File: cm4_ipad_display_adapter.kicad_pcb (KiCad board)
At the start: 4 copper layers, 16 parts, among them J1 Conn_01x22_Female, J3 Conn_01x34_Female, J4 Conn_01x03_Female, U1 SN65DSI83TPAPRQ1, U2 MIC5504-1.8YM5

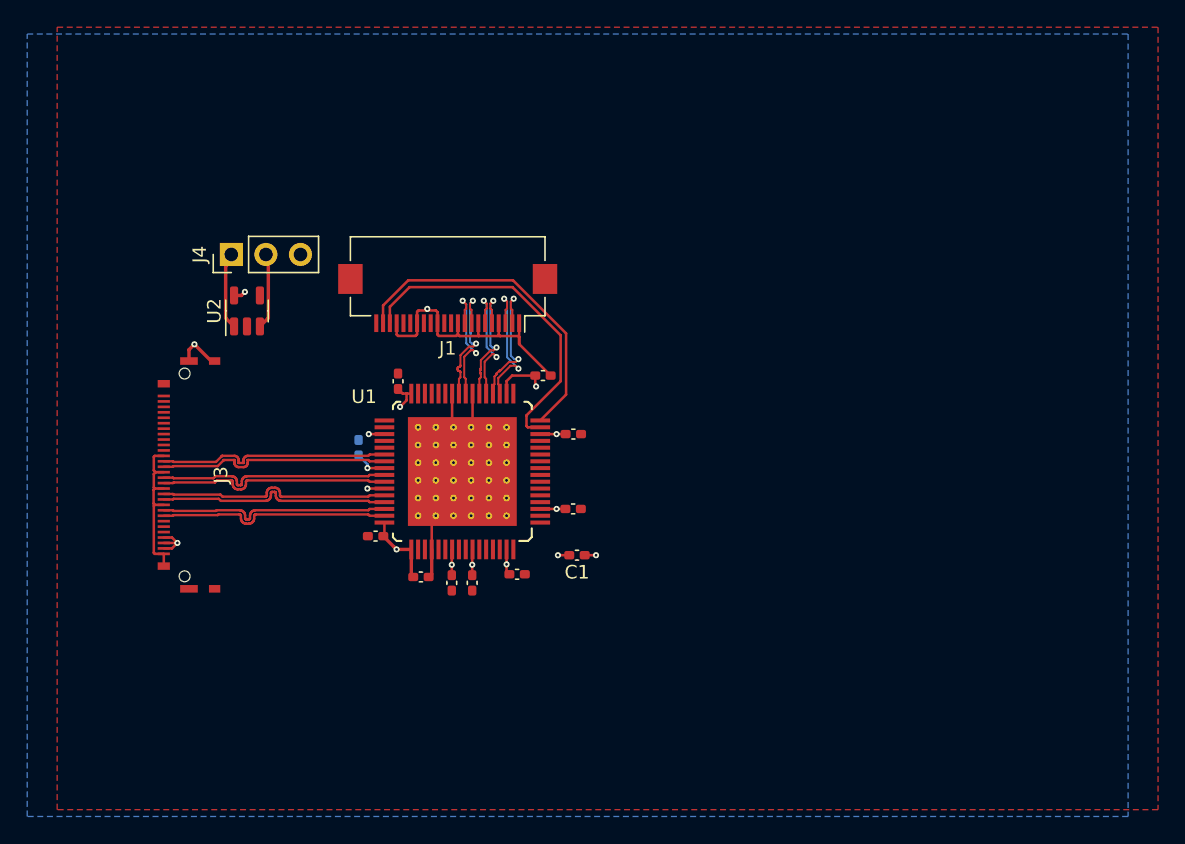
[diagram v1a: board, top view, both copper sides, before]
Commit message: Add footprints for LED driver HEAD associated components, route them. Fix DRC issues, and add an edge cut.
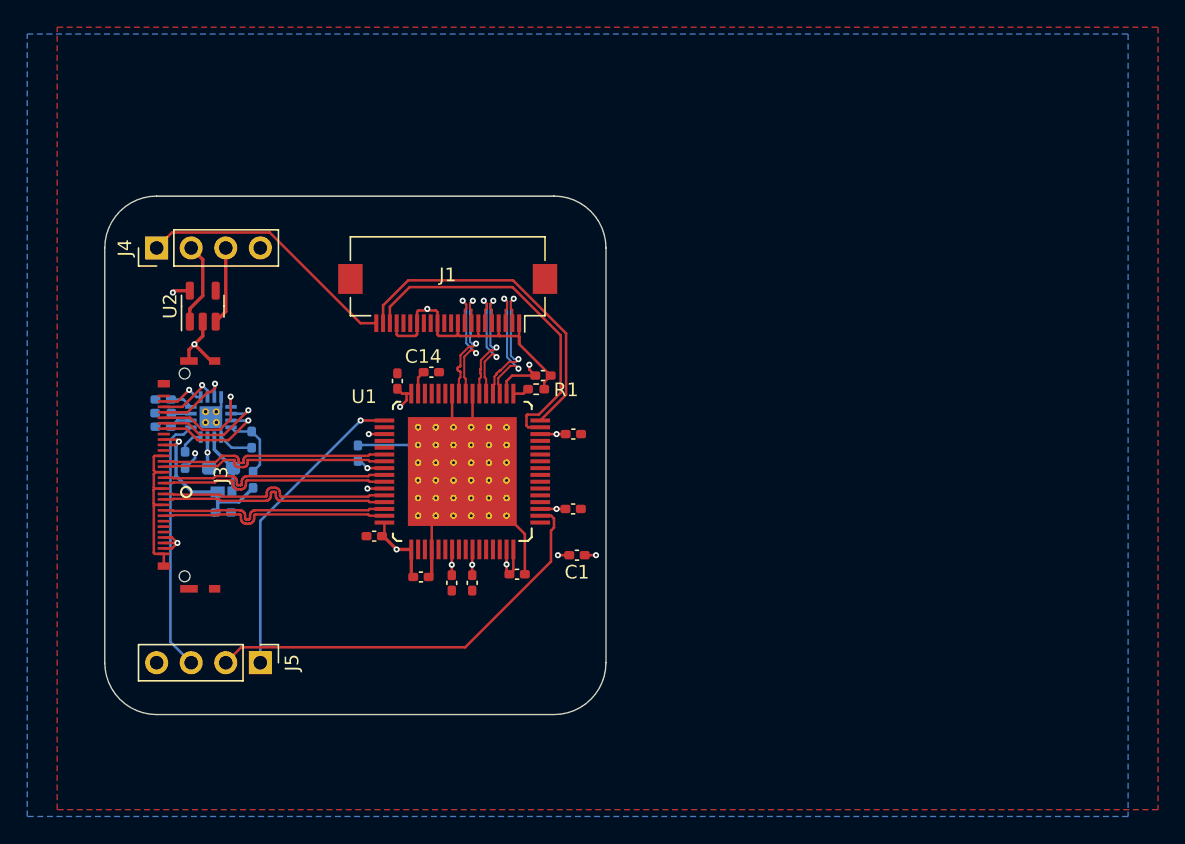
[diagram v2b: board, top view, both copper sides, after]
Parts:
- added C14: 1uF, Capacitor_SMD:C_0402_1005Metric_Pad0.74x0.62mm_HandSolder, F.Cu at (138.3, 54.9)
- added C15: 1uF, Capacitor_SMD:C_0402_1005Metric_Pad0.74x0.62mm_HandSolder, B.Cu at (118.6, 58.9)
- added C16: 0.47uF, Capacitor_SMD:C_0402_1005Metric_Pad0.74x0.62mm_HandSolder, B.Cu at (118.6, 56.9)
- added C17: 4.7uF, Capacitor_SMD:C_0402_1005Metric_Pad0.74x0.62mm_HandSolder, B.Cu at (123.0, 65.2)
- added D1: D_Schottky, footprints:PMEG4010EPK_315, B.Cu at (122.6, 63.7)
- added J5: Conn_01x04_Female, Connector_PinHeader_2.54mm:PinHeader_1x04_P2.54mm_Vertical, F.Cu at (125.7, 76.2)
- added L1: 4.7uH, Inductor_SMD:L_0603_1608Metric_Pad1.05x0.95mm_HandSolder, B.Cu at (122.8, 61.9)
- added R1: 10k, Resistor_SMD:R_0402_1005Metric_Pad0.72x0.64mm_HandSolder, F.Cu at (146.0, 56.1)
- added R2: 53.6k, Resistor_SMD:R_0402_1005Metric_Pad0.72x0.64mm_HandSolder, B.Cu at (118.6, 57.9)
- added R3: 1.3M, Resistor_SMD:R_0402_1005Metric_Pad0.72x0.64mm_HandSolder, B.Cu at (120.2, 61.3)
- added R4: 1M, Resistor_SMD:R_0402_1005Metric_Pad0.72x0.64mm_HandSolder, B.Cu at (125.2, 62.8)
- added R5: 143k, Resistor_SMD:R_0402_1005Metric_Pad0.72x0.64mm_HandSolder, B.Cu at (125.1, 59.8)
- added U3: TPS61176RTER, footprints:TPS61176RTER, B.Cu at (122.1, 58.1)
- J4: value Conn_01x03_Female -> Conn_01x02_Female; footprint Connector_PinHeader_2.54mm:PinHeader_1x03_P2.54mm_Vertical -> Connector_PinHeader_2.54mm:PinHeader_1x04_P2.54mm_Vertical
- U1: value SN65DSI83TPAPRQ1 -> PAP0064Q_N
- moved J4 5.51 mm to (118.1, 45.7)
- moved U2 3.27 mm to (121.5, 50.0)
- moved C5 0.40 mm to (132.9, 60.8)
- moved C2 0.10 mm to (134.1, 66.9)
- moved C4 0.05 mm to (135.8, 55.5)
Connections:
- J4 pad 2: Net-(J4-Pad2) -> VBAT
- J4 pad 3: GND -> LDO_EN
- U1 pad 17: unconnected-(U1-Pad17) -> Net-(R1-Pad1)
- U1 pad 2: unconnected-(U1-Pad2) -> Net-(J5-Pad2)
- U1 pad 31: unconnected-(U1-Pad31) -> Net-(C14-Pad1)
- U1 pad 33: unconnected-(U1-Pad33) -> Net-(J5-Pad1)
- U1 pad 64: unconnected-(U1-Pad64) -> VCC_1.8
- U2 pad 1: VCC_3.3 -> VBAT
- U2 pad 3: Net-(J4-Pad2) -> LDO_EN
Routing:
- net VCC_3.3: track 9.05 -> 45.0 mm
- net Net-(J5-Pad2): track 0.00 -> 31.3 mm
- net VBAT: track 0.00 -> 28.4 mm, vias 0 -> 1
- net Net-(J5-Pad1): track 0.00 -> 22.6 mm, vias 0 -> 1
- net PWM: track 0.00 -> 18.9 mm
- net GND: track 47.3 -> 66.2 mm, vias 3 -> 4
- net /LVDS/LED_ANODE: track 0.00 -> 13.8 mm, vias 0 -> 1
- net /LVDS/LED_CATHODE2: track 0.00 -> 8.70 mm, vias 0 -> 1
- net /LVDS/LED_CATHODE1: track 0.00 -> 8.44 mm, vias 0 -> 1
- net /LVDS/LED_CATHODE3: track 0.00 -> 8.01 mm, vias 0 -> 1
- net /LVDS/LED_CATHODE4: track 0.00 -> 5.81 mm, vias 0 -> 1
- net LDO_EN: track 0.00 -> 5.72 mm
- net Net-(J4-Pad2): track 5.62 -> 0.00 mm
- net Net-(R4-Pad2): track 0.00 -> 5.06 mm
- net Net-(L1-Pad2): track 0.00 -> 4.63 mm
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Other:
- board outline added: 36.8 x 38.1 mm

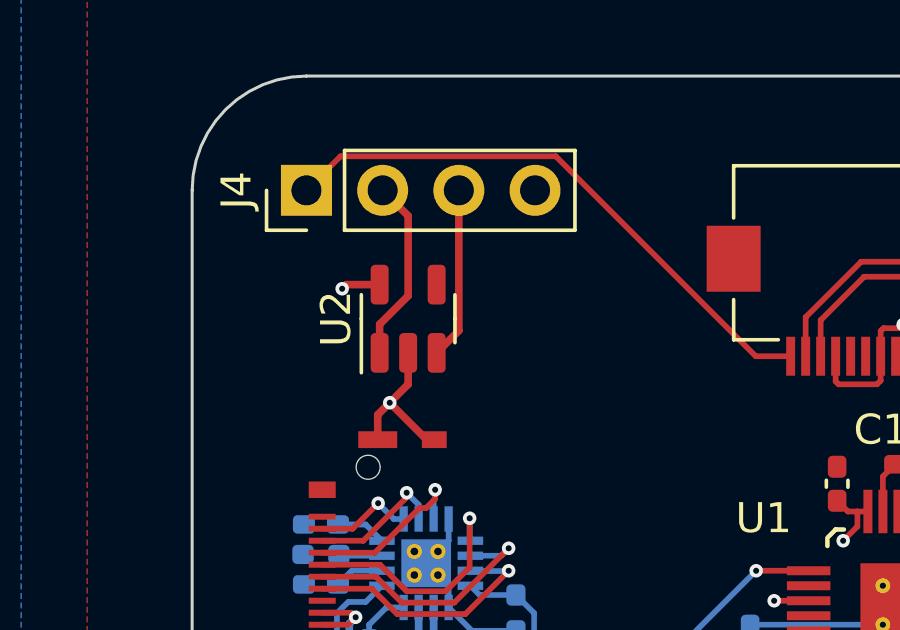
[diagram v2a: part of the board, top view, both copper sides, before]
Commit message: rearrange J4 pins to make traces for LDO simpler.
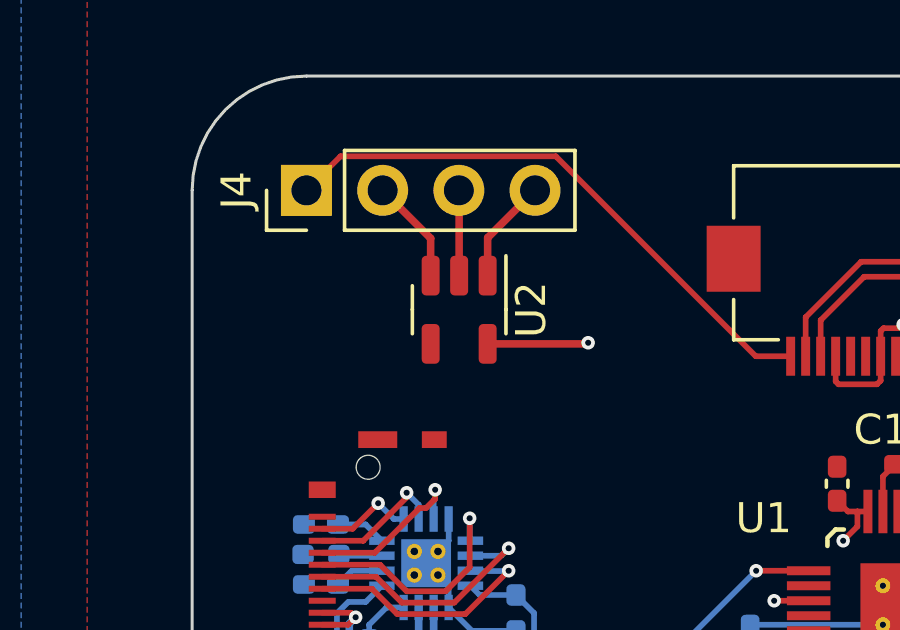
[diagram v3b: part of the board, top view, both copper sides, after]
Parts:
- U1: value PAP0064Q_N -> SN65DSI83TPAPRQ1
- moved U2 1.73 mm to (123.2, 49.7), turned to -90 degrees
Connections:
- net Net-(J5-Pad1) renamed /LVDS/IRQ
- net Net-(J5-Pad2) renamed /LVDS/SN65DSI83_EN
- J4 pad 2: VBAT -> LDO_EN
- J4 pad 3: LDO_EN -> GND
- J4 pad 4: GND -> VBAT
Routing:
- net VBAT: track 28.4 -> 23.7 mm
- net GND: track 66.2 -> 63.7 mm, vias 4 -> 3
- net LDO_EN: track 5.72 -> 3.51 mm
- net VCC_1.8: track 30.3 -> 32.4 mm
